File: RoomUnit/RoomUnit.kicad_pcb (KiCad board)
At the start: 2 copper layers, 9 parts, among them J4 Conn_01x03, U4 1.3

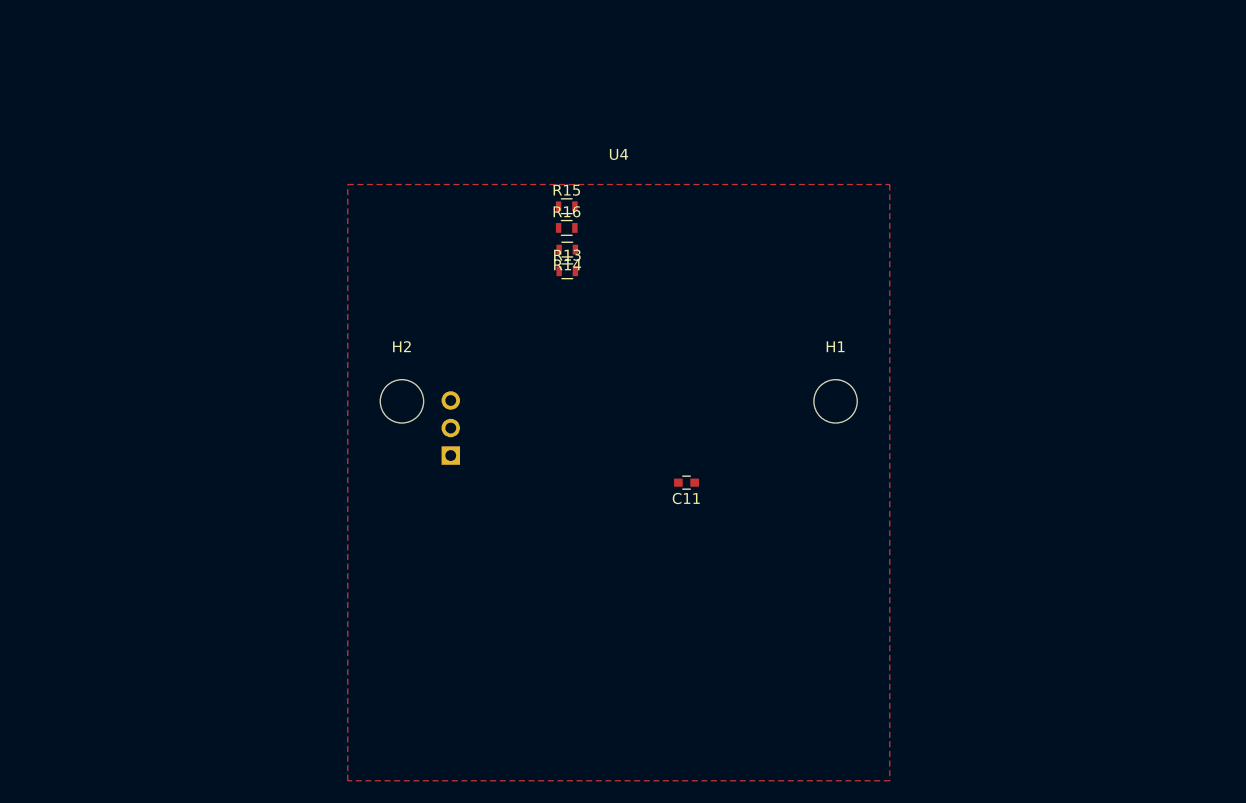
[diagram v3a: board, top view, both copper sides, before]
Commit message: Major work changing over to 868MHz solution. Current state unfinished
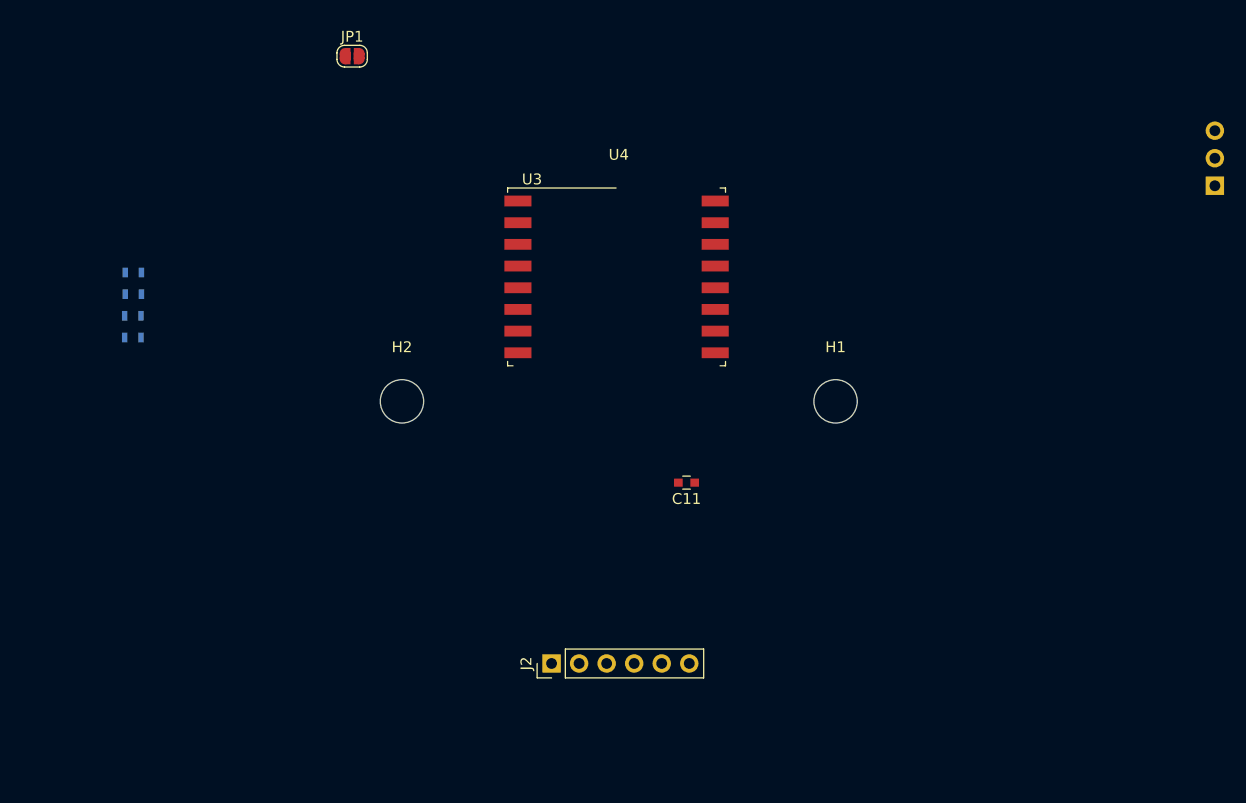
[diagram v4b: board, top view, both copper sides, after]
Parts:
- added J2: Conn_01x06_Female, Connector_PinHeader_2.54mm:PinHeader_1x06_P2.54mm_Vertical, F.Cu at (143.8, 124.2)
- added JP1: SolderJumper_2_Bridged, Jumper:SolderJumper-2_P1.3mm_Open_RoundedPad1.0x1.5mm, F.Cu at (125.4, 68.2)
- added U3: RFM69HW, RF_Module:HOPERF_RFM69HW, F.Cu at (149.8, 88.5)
- R13, R14, R15, R16: moved to B.Cu
- moved J4 74.8 mm to (205.0, 80.1)
- moved R13 40.5 mm to (105.2, 94.1), turned to 180 degrees
- moved R14 40.5 mm to (105.2, 92.1), turned to 0 degrees
- moved R15 40.4 mm to (105.2, 88.1), turned to 180 degrees
- moved R16 40.4 mm to (105.2, 90.1), turned to 180 degrees
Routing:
- removed copper zone on F.Cu, net GND

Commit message: Updates
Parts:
- added AE1: Antenna, Connector_PinHeader_2.54mm:PinHeader_1x01_P2.54mm_Horizontal, B.Cu at (138.0, 93.5)
- added BZ1: Buzzer, Buzzers_Beepers:Buzzer_12x9.5RM7.6, B.Cu at (153.2, 107.0)
- added C1: 10u, Capacitor_Tantalum_SMD:CP_EIA-3216-18_Kemet-A, F.Cu at (131.6, 91.1)
- added C2: 100n, Capacitors_SMD:C_0603, B.Cu at (96.2, 89.9)
- added C3: 10u, Capacitors_Tantalum_SMD:CP_Tantalum_Case-A_EIA-3216-18_Reflow, F.Cu at (131.6, 81.1)
- added C4: 10u, Capacitors_Tantalum_SMD:CP_Tantalum_Case-A_EIA-3216-18_Reflow, F.Cu at (131.6, 78.1)
- added C8: 100u, Capacitors_SMD:C_0603, F.Cu at (165.5, 110.1)
- added J1: Conn_01x02_Male, Connector_PinHeader_2.54mm:PinHeader_1x02_P2.54mm_Vertical, B.Cu at (165.8, 89.1)
- added J3: Conn_01x04_Male, Connector_JST:JST_SH_BM04B-SRSS-TB_1x04-1MP_P1.00mm_Vertical, F.Cu at (168.7, 82.2)
- added Q1: BC817, TO_SOT_Packages_SMD:SOT-23, F.Cu at (154.5, 110.8)
- added R12: 2k2, Resistors_SMD:R_0603, F.Cu at (157.8, 109.8)
- added R5: 10k, Resistors_SMD:R_0603, B.Cu at (95.9, 88.1)
- added R6: 10k, Resistors_SMD:R_0603, B.Cu at (105.1, 100.1)
- added R7: 10k, Resistors_SMD:R_0603, B.Cu at (95.9, 92.1)
- added R8: 10k, Resistors_SMD:R_0603, F.Cu at (160.4, 89.1)
- added R9: 10k, Resistors_SMD:R_0603, B.Cu at (105.1, 98.1)
- added U1: LM1117-3.3, TO_SOT_Packages_SMD:SOT-223-3_TabPin2, F.Cu at (131.6, 86.1)
- added U2: ESP-12F, RF_Modules:ESP-12E, F.Cu at (149.8, 84.6)
- added U5: LTR-303ALS-01, Opto-Devices:Lite-On_LTR-303ALS-01, F.Cu at (168.0, 110.0)
- J4: value Conn_01x03 -> Screw_Terminal_01x02; footprint Pin_Headers:Pin_Header_Straight_1x03_Pitch2.54mm -> TerminalBlock_Phoenix:TerminalBlock_Phoenix_MPT-0,5-2-2.54_1x02_P2.54mm_Horizontal
- R15, R16: moved to F.Cu
- U3: moved to B.Cu
- U4: value 1.3 -> 1.3"_128x64OLED_I2C
- moved J4 80.1 mm to (129.9, 107.8), turned to -90 degrees
- moved R15 55.6 mm to (160.4, 81.1), turned to 0 degrees
- moved R16 55.6 mm to (160.4, 83.1), turned to 0 degrees
- moved JP1 23.6 mm to (127.7, 91.7), turned to 90 degrees
- moved U4 1.32 mm to (149.7, 101.0)
- turned U3 to 180 degrees
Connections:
- J4 pad 1: Net-(J4-Pad1) -> GND
- J4 pad 2: Net-(J4-Pad2) -> +5V
- R15 pad 2: Net-(J4-Pad2) -> Net-(J3-Pad2)
- R16 pad 2: Net-(J4-Pad1) -> Net-(J3-Pad3)
- U3 pad 1: Net-(U3-Pad1) -> unconnected-(U3-Pad1)
- U3 pad 12: Net-(U3-Pad12) -> unconnected-(U3-Pad12)
- U3 pad 13: Net-(U3-Pad13) -> unconnected-(U3-Pad13)
- U3 pad 14: Net-(U3-Pad14) -> unconnected-(U3-Pad14)
- U3 pad 15: Net-(U3-Pad15) -> unconnected-(U3-Pad15)
- U3 pad 16: Net-(U3-Pad16) -> unconnected-(U3-Pad16)
- U3 pad 2: Net-(U3-Pad2) -> unconnected-(U3-Pad2)
- U3 pad 3: Net-(U3-Pad3) -> unconnected-(U3-Pad3)
- U3 pad 4: Net-(U3-Pad4) -> unconnected-(U3-Pad4)
- U3 pad 5: Net-(U3-Pad5) -> unconnected-(U3-Pad5)
- U3 pad 6: Net-(U3-Pad6) -> unconnected-(U3-Pad6)
- U3 pad 7: Net-(U3-Pad7) -> unconnected-(U3-Pad7)
- U3 pad 8: Net-(U3-Pad8) -> unconnected-(U3-Pad8)
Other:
- board outline added: 70 x 70 mm
- net class Default removed
- board text added: "FLASH"
- board text added: "RUN"
- board text added: "RX"
- board text added: "TX"
